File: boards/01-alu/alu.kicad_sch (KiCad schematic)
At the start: 228 parts, among them J1 BUS, Q1 2N7000, Q10 2N7000, Q100 2N7000, Q101 2N7000, Q102 2N7000, Q103 2N7000, Q104 2N7000, Q105 2N7000, Q106 2N7000, Q107 2N7000, Q108 2N7000, Q109 2N7000, Q11 2N7000, Q110 2N7000, Q111 2N7000, Q112 2N7000, Q113 2N7000, Q114 2N7000, Q115 2N7000, Q116 2N7000, Q117 2N7000, Q118 2N7000, Q119 2N7000, Q12 2N7000, Q120 2N7000, Q121 2N7000, Q122 2N7000, Q123 2N7000, Q124 2N7000, Q125 2N7000, Q126 2N7000, Q127 2N7000, Q128 2N7000, Q129 2N7000, Q13 2N7000, Q130 2N7000, Q131 2N7000, Q132 2N7000, Q133 2N7000, Q134 2N7000, Q135 2N7000, Q136 2N7000, Q137 2N7000, Q14 2N7000, Q15 2N7000, Q16 2N7000, Q17 2N7000, Q18 2N7000, Q19 2N7000, Q2 2N7000, Q20 2N7000, Q21 2N7000, Q22 2N7000, Q23 2N7000, Q24 2N7000, Q25 2N7000, Q26 2N7000, Q27 2N7000, Q28 2N7000, Q29 2N7000, Q3 2N7000, Q30 2N7000, Q31 2N7000, Q32 2N7000, Q33 2N7000, Q34 2N7000, Q35 2N7000, Q36 2N7000, Q37 2N7000, Q38 2N7000, Q39 2N7000, Q4 2N7000, Q40 2N7000, Q41 2N7000, Q42 2N7000, Q43 2N7000, Q44 2N7000, Q45 2N7000, Q46 2N7000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

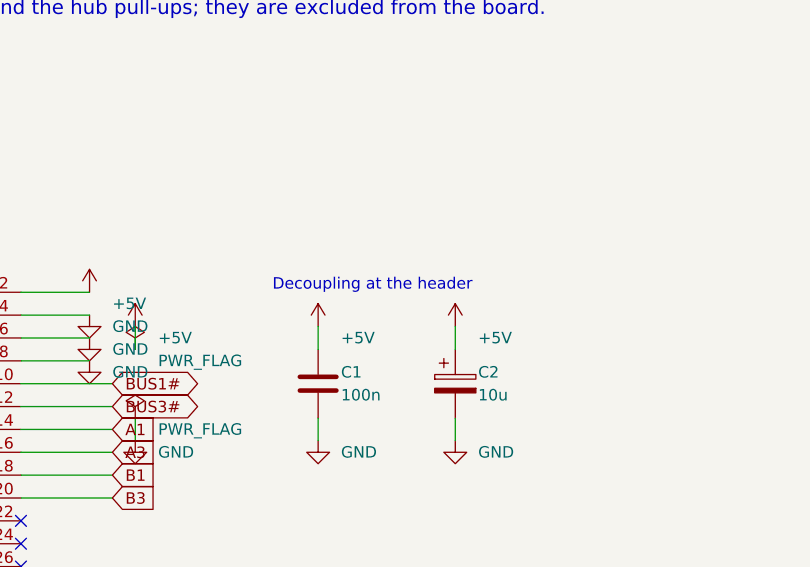
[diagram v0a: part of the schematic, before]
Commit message: Coupon, ALU and hub PCBs routed and DRC clean; fab outputs
pcb.py: power pre-routed as per-column rails from the tile geometry, fixed in
the DSN so the router cannot move them; GND pour before routing; DRC-verified
ground stitching; inset outline while routing; retries until zero unconnected.
Coupon 112x94, ALU 156x214, hub 130x98 mm. docs/bring-up.md and docs/order-1.md.

Co-Authored-By: Claude Fable 5.1 <noreply@anthropic.com>
Claude-Session: https://claude.ai/code/session_019vcbW37ERmrjZaWq55Er3J
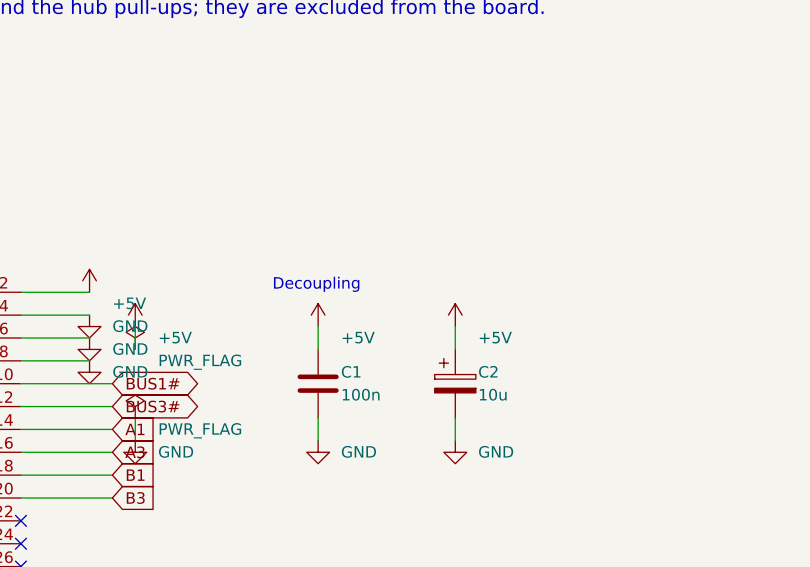
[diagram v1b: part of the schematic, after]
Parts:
- H1, H2, H3, H4: footprint MountingHole:MountingHole_3.2mm_M3 -> MountingHole:MountingHole_3.2mm_M3_Pad
- Q1, Q10, Q100, Q101, Q102, Q103, Q104, Q105, Q106, Q107, Q108, Q109, Q11, Q110, Q111, Q112, Q113, Q114, Q115, Q116, Q117, Q118, Q119, Q12, Q120, Q121, Q122, Q123, Q124, Q125, Q126, Q127, Q128, Q129, Q13, Q130, Q131, Q132, Q133, Q134, Q135, Q136, Q137, Q14, Q15, Q16, Q17, Q18, Q19, Q2, Q20, Q21, Q22, Q23, Q24, Q25, Q26, Q27, Q28, Q29, Q3, Q30, Q31, Q32, Q33, Q34, Q35, Q36, Q37, Q38, Q39, Q4, Q40, Q41, Q42, Q43, Q44, Q45, Q46, Q47, Q48, Q49, Q5, Q50, Q51, Q52, Q53, Q54, Q55, Q56, Q57, Q58, Q59, Q6, Q60, Q61, Q62, Q63, Q64, Q65, Q66, Q67, Q68, Q69, Q7, Q70, Q71, Q72, Q73, Q74, Q75, Q76, Q77, Q78, Q79, Q8, Q80, Q81, Q82, Q83, Q84, Q85, Q86, Q87, Q88, Q89, Q9, Q90, Q91, Q92, Q93, Q94, Q95, Q96, Q97, Q98, Q99: footprint Package_TO_SOT_THT:TO-92_Inline -> Package_TO_SOT_THT:TO-92_Inline_Wide
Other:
- note added: "Decoupling"
- note removed: "Decoupling at the header"

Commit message: ALU v2: ONE, F0 and F1 lines give INC/DEC, AND, OR and XOR; exhaustive at four corners
233 transistors. ONE forces the B operand to 1 for INC and DEC; F1:F0 select
add/sub, and, or, xor per bit through a result mux. Testbench rewritten
around (a, b, ctl) cases and vectorised scoring; the kicad-cli export passes
all 2,304 cases at TYP, LO, HI and the mixed-threshold corner.

Co-Authored-By: Claude Fable 5.1 <noreply@anthropic.com>
Claude-Session: https://claude.ai/code/session_019vcbW37ERmrjZaWq55Er3J
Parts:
- removed J1: BUS, Connector_IDC:IDC-Header_2x25_P2.54mm_Vertical, symbol Connector_Generic:Conn_02x25_Odd_Even
- added J1: BUS, Connector_IDC:IDC-Header_2x32_P2.54mm_Vertical, symbol Connector_Generic:Conn_02x32_Odd_Even
- added Q138, Q139, Q140, Q141, Q142, Q143, Q144, Q145, Q146, Q147, Q148, Q149, Q150, Q151, Q152, Q153, Q154, Q155, Q156, Q157, Q158, Q159, Q160, Q161, Q162, Q163, Q164, Q165, Q166, Q167, Q168, Q169, Q170, Q171, Q172, Q173, Q174, Q175, Q176, Q177, Q178, Q179, Q180, Q181, Q182, Q183, Q184, Q185, Q186, Q187, Q188, Q189, Q190, Q191, Q192, Q193, Q194, Q195, Q196, Q197, Q198, Q199, Q200, Q201, Q202, Q203, Q204, Q205, Q206, Q207, Q208, Q209, Q210, Q211, Q212, Q213, Q214, Q215, Q216, Q217, Q218, Q219, Q220, Q221, Q222, Q223, Q224, Q225, Q226, Q227, Q228, Q229, Q230, Q231, Q232, Q233: 2N7000, Package_TO_SOT_THT:TO-92_Inline_Wide, symbol Transistor_FET:2N7000
- added R100, R101, R102, R103, R104, R105, R106, R107, R108, R109, R110, R111, R112, R113, R114, R115, R116, R117, R118, R119, R120, R121, R122, R123, R124, R125, R126, R127, R79, R80, R81, R82, R83, R84, R85, R86, R87, R88, R89, R90, R91, R92, R93, R94, R95, R96, R97, R98, R99: 47k, Resistor_THT:R_Axial_DIN0207_L6.3mm_D2.5mm_P5.08mm_Vertical, symbol Device:R
- added R128, R129, R130, R131, R132, R133: 1k, Resistor_THT:R_Axial_DIN0207_L6.3mm_D2.5mm_P5.08mm_Vertical, symbol Device:R
- R73, R74, R75, R76, R77, R78: value 1k -> 47k
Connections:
- net +5V: now also J1.1 (Pin_1), J1.2 (Pin_2), J1.63 (Pin_63), R100.1, R101.1, R102.1, R103.1, R104.1, R105.1, R106.1, R107.1, R108.1, R109.1, R110.1, R111.1, R112.1, R113.1, R114.1, R115.1, R116.1, R117.1, R118.1, R119.1, R120.1, R121.1, R122.1, R123.1, R124.1, R125.1, R126.1, R127.1, R128.1, R129.1, R130.1, R131.1, R132.1, R133.1, R79.1, R80.1, R81.1, R82.1, R83.1, R84.1, R85.1, R86.1, R87.1, R88.1, R89.1, R90.1, R91.1, R92.1, R93.1, R94.1, R95.1, R96.1, R97.1, R98.1, R99.1
- net A0: now also Q42.2 (G), Q56.2 (G), J1.13 (Pin_13); no longer Q30.2 (G), Q32.2 (G)
- net A1: now also Q62.2 (G), Q76.2 (G), J1.14 (Pin_14); no longer Q50.2 (G), Q52.2 (G)
- net A2: now also Q82.2 (G), Q96.2 (G), J1.15 (Pin_15); no longer Q70.2 (G), Q72.2 (G)
- net A3: now also Q102.2 (G), Q116.2 (G), J1.16 (Pin_16); no longer Q90.2 (G), Q92.2 (G)
- net B0: now also J1.17 (Pin_17)
- net B1: now also Q12.2 (G), J1.18 (Pin_18); no longer Q10.2 (G), Q9.2 (G)
- net B2: now also Q22.2 (G), J1.19 (Pin_19); no longer Q16.2 (G), Q17.2 (G)
- net B3: now also Q32.2 (G), J1.20 (Pin_20); no longer Q23.2 (G), Q24.2 (G)
- net BD0: now also Q214.3 (D), Q215.2 (G), R121.2; no longer Q118.3 (D), Q119.2 (G), R66.2
- net BD1: now also Q218.3 (D), Q219.2 (G), R123.2; no longer Q122.3 (D), Q123.2 (G), R68.2
- net BD2: now also Q222.3 (D), Q223.2 (G), R125.2; no longer Q126.3 (D), Q127.2 (G), R70.2
- net BD3: now also Q226.3 (D), Q227.2 (G), R127.2; no longer Q130.3 (D), Q131.2 (G), R72.2
- net BDN0: now also Q212.3 (D), Q214.2 (G), R120.2; no longer Q116.3 (D), Q118.2 (G), R65.2
- net BDN1: now also Q216.3 (D), Q218.2 (G), R122.2; no longer Q120.3 (D), Q122.2 (G), R67.2
- net BDN2: now also Q220.3 (D), Q222.2 (G), R124.2; no longer Q124.3 (D), Q126.2 (G), R69.2
- net BDN3: now also Q224.3 (D), Q226.2 (G), R126.2; no longer Q128.3 (D), Q130.2 (G), R71.2
- net BN0: no longer Q5.2 (G)
- net BN1: now also Q12.3 (D), Q13.2 (G), R8.2; no longer Q12.2 (G), Q9.3 (D), R6.2
- net BN2: now also Q22.3 (D), Q23.2 (G), R14.2; no longer Q16.3 (D), Q19.2 (G), R10.2
- net BN3: now also Q32.3 (D), Q33.2 (G), R20.2; no longer Q23.3 (D), Q26.2 (G), R14.2
- net BUS0#: now also J1.9 (Pin_9), Q215.3 (D); no longer Q119.3 (D)
- net BUS1#: now also J1.10 (Pin_10), Q219.3 (D); no longer Q123.3 (D)
- net BUS2#: now also J1.11 (Pin_11), Q223.3 (D); no longer Q127.3 (D)
- net BUS3#: now also J1.12 (Pin_12), Q227.3 (D); no longer Q131.3 (D)
- net C1: now also Q60.3 (D), Q70.2 (G), Q72.2 (G), Q79.2 (G), R36.2; no longer Q48.3 (D), Q58.2 (G), Q60.2 (G), Q67.2 (G), R28.2
- net C2: now also Q80.3 (D), Q90.2 (G), Q92.2 (G), Q99.2 (G), R47.2; no longer Q68.3 (D), Q78.2 (G), Q80.2 (G), Q87.2 (G), R39.2
- net C3: now also Q100.3 (D), Q110.2 (G), Q112.2 (G), Q119.2 (G), R58.2; no longer Q100.2 (G), Q107.2 (G), Q88.3 (D), Q98.2 (G), R50.2
- net C4: now also Q120.3 (D), R69.2, Q205.2 (G); no longer Q108.3 (D), Q111.2 (G), R61.2
- net CF: now also J1.37 (Pin_37), Q207.3 (D), Q232.2 (G), R118.2; no longer Q110.3 (D), Q136.2 (G), R62.2
- net EO: now also J1.40 (Pin_40), Q213.2 (G), Q217.2 (G), Q221.2 (G), Q225.2 (G); no longer Q117.2 (G), Q121.2 (G), Q125.2 (G), Q129.2 (G)
- net G0: now also Q133.2 (G), Q136.2 (G), Q56.3 (D), Q60.2 (G), R34.2; no longer Q44.3 (D), Q48.2 (G), R26.2
- net G1: now also Q76.3 (D), Q80.2 (G), R45.2, Q151.2 (G), Q154.2 (G); no longer Q64.3 (D), Q68.2 (G), R37.2
- net G2: now also Q100.2 (G), Q96.3 (D), R56.2, Q169.2 (G), Q172.2 (G); no longer Q84.3 (D), Q88.2 (G), R48.2
- net G3: now also Q116.3 (D), Q120.2 (G), R67.2, Q187.2 (G), Q190.2 (G); no longer Q104.3 (D), Q108.2 (G), R59.2
- net GND: now also Q106.1 (S), Q108.1 (S), Q12.1 (S), Q124.1 (S), Q128.1 (S), Q14.1 (S), Q17.1 (S), Q19.1 (S), Q21.1 (S), Q24.1 (S), Q3.1 (S), Q32.1 (S), Q39.1 (S), Q46.1 (S), Q48.1 (S), Q5.1 (S), Q52.1 (S), Q59.1 (S), Q66.1 (S), Q68.1 (S), Q7.1 (S), Q72.1 (S), Q79.1 (S), Q86.1 (S), Q88.1 (S), Q92.1 (S), Q99.1 (S), J1.3 (Pin_3), J1.4 (Pin_4), J1.6 (Pin_6), J1.64 (Pin_64), J1.8 (Pin_8), Q138.1 (S), Q140.1 (S), Q142.1 (S), Q144.1 (S), Q147.1 (S), Q148.1 (S), Q150.1 (S), Q151.1 (S), Q152.1 (S), Q154.1 (S), Q156.1 (S), Q158.1 (S), Q160.1 (S), Q162.1 (S), Q165.1 (S), Q166.1 (S), Q168.1 (S), Q169.1 (S), Q170.1 (S), Q172.1 (S), Q174.1 (S), Q176.1 (S), Q178.1 (S), Q180.1 (S), Q183.1 (S), Q184.1 (S), Q186.1 (S), Q187.1 (S), Q188.1 (S), Q190.1 (S), Q192.1 (S), Q194.1 (S), Q196.1 (S), Q198.1 (S), Q201.1 (S), Q202.1 (S), Q204.1 (S), Q206.1 (S), Q207.1 (S), Q208.1 (S), Q209.1 (S), Q210.1 (S), Q211.1 (S), Q213.1 (S), Q214.1 (S), Q215.1 (S), Q217.1 (S), Q218.1 (S), Q219.1 (S), Q221.1 (S), Q222.1 (S), Q223.1 (S), Q225.1 (S), Q226.1 (S), Q227.1 (S), Q228.1 (S), Q229.1 (S), Q230.1 (S), Q231.1 (S), Q232.1 (S), Q233.1 (S); no longer Q100.1 (S), Q111.1 (S), Q118.1 (S), Q130.1 (S), Q135.1 (S), Q137.1 (S), Q16.1 (S), Q18.1 (S), Q20.1 (S), Q30.1 (S), Q36.1 (S), Q38.1 (S), Q40.1 (S), Q51.1 (S), Q56.1 (S), Q58.1 (S), Q6.1 (S), Q60.1 (S), Q71.1 (S), Q76.1 (S), Q78.1 (S), Q8.1 (S), Q80.1 (S), Q91.1 (S), Q96.1 (S), Q98.1 (S)
- net P0: now also Q134.2 (G), Q47.3 (D), Q48.3 (D), Q49.2 (G), Q51.2 (G), Q58.2 (G), R29.2, Q144.2 (G); no longer Q35.3 (D), Q36.3 (D), Q37.2 (G), Q39.2 (G), Q46.2 (G), R21.2
- net P0_a: now also Q44.3 (D), Q46.2 (G), R27.2; no longer Q32.3 (D), Q34.2 (G), R19.2
- net P0_d: now also Q46.3 (D), Q48.2 (G), R28.2; no longer Q34.3 (D), Q36.2 (G), R20.2
- net P0_n: now also Q42.3 (D), Q43.3 (D), Q47.2 (G), R26.2; no longer Q30.3 (D), Q31.3 (D), Q35.2 (G), R18.2
- net P1: now also Q67.3 (D), Q68.3 (D), Q69.2 (G), Q71.2 (G), Q78.2 (G), R40.2, Q152.2 (G), Q162.2 (G); no longer Q55.3 (D), Q56.3 (D), Q57.2 (G), Q59.2 (G), Q66.2 (G), R32.2
- net P1_a: now also Q64.3 (D), Q66.2 (G), R38.2; no longer Q52.3 (D), Q54.2 (G), R30.2
- net P1_d: now also Q66.3 (D), Q68.2 (G), R39.2; no longer Q54.3 (D), Q56.2 (G), R31.2
- net P1_n: now also Q62.3 (D), Q63.3 (D), Q67.2 (G), R37.2; no longer Q50.3 (D), Q51.3 (D), Q55.2 (G), R29.2
- net P2: now also Q87.3 (D), Q88.3 (D), Q89.2 (G), Q91.2 (G), Q98.2 (G), R51.2, Q170.2 (G), Q180.2 (G); no longer Q75.3 (D), Q76.3 (D), Q77.2 (G), Q79.2 (G), Q86.2 (G), R43.2
- net P2_a: now also Q84.3 (D), Q86.2 (G), R49.2; no longer Q72.3 (D), Q74.2 (G), R41.2
- net P2_d: now also Q86.3 (D), Q88.2 (G), R50.2; no longer Q74.3 (D), Q76.2 (G), R42.2
- net P2_n: now also Q82.3 (D), Q83.3 (D), Q87.2 (G), R48.2; no longer Q70.3 (D), Q71.3 (D), Q75.2 (G), R40.2
- net P3: now also Q107.3 (D), Q108.3 (D), Q109.2 (G), Q111.2 (G), Q118.2 (G), R62.2, Q188.2 (G), Q198.2 (G); no longer Q106.2 (G), Q95.3 (D), Q96.3 (D), Q97.2 (G), Q99.2 (G), R54.2
- net P3_a: now also Q104.3 (D), Q106.2 (G), R60.2; no longer Q92.3 (D), Q94.2 (G), R52.2
- net P3_d: now also Q106.3 (D), Q108.2 (G), R61.2; no longer Q94.3 (D), Q96.2 (G), R53.2
- net P3_n: now also Q102.3 (D), Q103.3 (D), Q107.2 (G), R59.2; no longer Q90.3 (D), Q91.3 (D), Q95.2 (G), R51.2
- net S0: now also Q54.3 (D), Q55.3 (D), R33.2, Q138.2 (G); no longer Q112.2 (G), Q116.2 (G), Q135.2 (G), Q42.3 (D), Q43.3 (D), R25.2
- net S0_a: now also Q51.3 (D), Q53.2 (G), R31.2; no longer Q39.3 (D), Q41.2 (G), R23.2
- net S0_d: now also Q53.3 (D), Q55.2 (G), R32.2; no longer Q41.3 (D), Q43.2 (G), R24.2
- net S0_n: now also Q49.3 (D), Q50.3 (D), Q54.2 (G), R30.2; no longer Q37.3 (D), Q38.3 (D), Q42.2 (G), R22.2
- net S1: now also Q74.3 (D), Q75.3 (D), R44.2, Q156.2 (G); no longer Q113.2 (G), Q120.2 (G), Q134.2 (G), Q62.3 (D), Q63.3 (D), R36.2
- net S1_a: now also Q71.3 (D), Q73.2 (G), R42.2; no longer Q59.3 (D), Q61.2 (G), R34.2
- net S1_d: now also Q73.3 (D), Q75.2 (G), R43.2; no longer Q61.3 (D), Q63.2 (G), R35.2
- net S1_n: now also Q69.3 (D), Q70.3 (D), Q74.2 (G), R41.2; no longer Q57.3 (D), Q58.3 (D), Q62.2 (G), R33.2
- net S2: now also Q94.3 (D), Q95.3 (D), R55.2, Q174.2 (G); no longer Q114.2 (G), Q124.2 (G), Q133.2 (G), Q82.3 (D), Q83.3 (D), R47.2
- net S2_a: now also Q91.3 (D), Q93.2 (G), R53.2; no longer Q79.3 (D), Q81.2 (G), R45.2
- net S2_d: now also Q93.3 (D), Q95.2 (G), R54.2; no longer Q81.3 (D), Q83.2 (G), R46.2
- net S2_n: now also Q89.3 (D), Q90.3 (D), Q94.2 (G), R52.2; no longer Q77.3 (D), Q78.3 (D), Q82.2 (G), R44.2
- net S3: now also Q114.3 (D), Q115.3 (D), R66.2, Q192.2 (G); no longer Q102.3 (D), Q103.3 (D), Q115.2 (G), Q128.2 (G), Q132.2 (G), R58.2
- net S3_a: now also Q111.3 (D), Q113.2 (G), R64.2; no longer Q101.2 (G), Q99.3 (D), R56.2
- net S3_d: now also Q113.3 (D), Q115.2 (G), R65.2; no longer Q101.3 (D), Q103.2 (G), R57.2
- net S3_n: now also Q109.3 (D), Q110.3 (D), Q114.2 (G), R63.2; no longer Q102.2 (G), Q97.3 (D), Q98.3 (D), R55.2
- net SUB: now also Q19.2 (G), Q29.2 (G), Q39.2 (G), Q50.2 (G), Q52.2 (G), Q59.2 (G), Q9.2 (G), J1.39 (Pin_39); no longer Q13.2 (G), Q20.2 (G), Q27.2 (G), Q38.2 (G), Q40.2 (G), Q47.2 (G), Q6.2 (G)
- net SUBN: now also Q17.2 (G), Q27.2 (G), Q37.2 (G), Q7.2 (G); no longer Q11.2 (G), Q18.2 (G), Q25.2 (G), Q4.2 (G)
- net T0: now also Q58.3 (D), Q61.2 (G), R35.2; no longer Q46.3 (D), Q49.2 (G), R27.2
- net T1: now also Q78.3 (D), Q81.2 (G), R46.2; no longer Q66.3 (D), Q69.2 (G), R38.2
- net T2: now also Q101.2 (G), Q98.3 (D), R57.2; no longer Q86.3 (D), Q89.2 (G), R49.2
- net T3: now also Q118.3 (D), Q121.2 (G), R68.2; no longer Q106.3 (D), Q109.2 (G), R60.2
- net XB0: now also Q10.3 (D), Q43.2 (G), Q57.2 (G), R7.2; no longer Q31.2 (G), Q33.2 (G), Q7.3 (D), R5.2
- net XB1: now also Q20.3 (D), Q63.2 (G), Q77.2 (G), R13.2; no longer Q14.3 (D), Q51.2 (G), Q53.2 (G), R9.2
- net XB2: now also Q30.3 (D), Q83.2 (G), Q97.2 (G), R19.2; no longer Q21.3 (D), Q71.2 (G), Q73.2 (G), R13.2
- net XB3: now also Q103.2 (G), Q117.2 (G), Q40.3 (D), R25.2; no longer Q28.3 (D), Q91.2 (G), Q93.2 (G), R17.2
- net XBA0: now also Q10.2 (G), Q6.3 (D), R5.2; no longer Q3.3 (D), Q7.2 (G), R3.2
- net XBA1: now also Q16.3 (D), Q20.2 (G), R11.2; no longer Q10.3 (D), Q14.2 (G), R7.2
- net XBA2: now also Q26.3 (D), Q30.2 (G), R17.2; no longer Q17.3 (D), Q21.2 (G), R11.2
- net XBA3: now also Q36.3 (D), Q40.2 (G), R23.2; no longer Q24.3 (D), Q28.2 (G), R15.2
- net XBB0: now also Q11.2 (G), Q8.3 (D), R6.2; no longer Q5.3 (D), Q8.2 (G), R4.2
- net XBB1: now also Q18.3 (D), Q21.2 (G), R12.2; no longer Q12.3 (D), Q15.2 (G), R8.2
- net XBB2: now also Q28.3 (D), Q31.2 (G), R18.2; no longer Q19.3 (D), Q22.2 (G), R12.2
- net XBB3: now also Q38.3 (D), Q41.2 (G), R24.2; no longer Q26.3 (D), Q29.2 (G), R16.2
- net ZF: now also J1.38 (Pin_38), Q208.3 (D), Q209.3 (D), Q210.3 (D), Q211.3 (D), Q233.2 (G), R119.2; no longer Q112.3 (D), Q113.3 (D), Q114.3 (D), Q115.3 (D), Q137.2 (G), R64.2
- net at D5.2 (A): now also R132.2; no longer R77.2
- net BB1N: now reaches Q15.3 (D)
- net BB1N: now also Q18.2 (G), R10.2; no longer Q14.1 (S)
- net at D1.2 (A): now also R128.2; no longer R73.2
- net BB2N: now reaches Q25.3 (D)
- net BB2N: now also Q28.2 (G), R16.2; no longer Q24.1 (S)
- net at D1.1 (K): now also Q228.3 (D); no longer Q132.3 (D)
- net at D5.1 (K): now also Q232.3 (D); no longer Q136.3 (D)
- net BB0N: now reaches Q4.3 (D)
- net BB0N: now also Q3.3 (D), Q5.2 (G), Q8.2 (G), R3.2; no longer Q3.1 (S)
- net BB3: now reaches Q33.3 (D)
- net BB3: now also Q34.3 (D), Q35.2 (G), Q36.2 (G), R21.2; no longer Q32.1 (S)
- net at D2.1 (K): now also Q229.3 (D); no longer Q133.3 (D)
- net at D2.2 (A): now also R129.2; no longer R74.2
- net at D4.1 (K): now also Q231.3 (D); no longer Q135.3 (D)
- net at D4.2 (A): now also R131.2; no longer R76.2
- net FS: now reaches Q125.3 (D)
- net FS: now also Q124.3 (D), Q137.2 (G), R72.2, Q155.2 (G), Q173.2 (G), Q191.2 (G), Q206.2 (G); no longer Q124.1 (S)
- net at D6.1 (K): now also Q233.3 (D); no longer Q137.3 (D)
- net FO: now reaches Q129.3 (D)
- net FO: now also Q128.3 (D), R74.2, Q141.2 (G), Q159.2 (G), Q177.2 (G), Q195.2 (G); no longer Q128.1 (S)
- net at D6.2 (A): now also R133.2; no longer R78.2
- net at D3.1 (K): now also Q230.3 (D); no longer Q134.3 (D)
- net BB1: now reaches Q13.3 (D)
- net BB1: now also Q14.3 (D), Q15.2 (G), Q16.2 (G), R9.2; no longer Q12.1 (S)
- net at D3.2 (A): now also R130.2; no longer R75.2
- removed net C4N: Q110.2 (G), Q111.3 (D), R63.2
- new net: Q130.1 (S), Q131.3 (D)
- new net: Q189.1 (S), Q190.3 (D)
- new net: Q60.1 (S), Q61.3 (D)
- new net: Q139.1 (S), Q140.3 (D)
- new net: Q212.1 (S), Q213.3 (D)
- new net: Q195.1 (S), Q196.3 (D)
- new net: Q36.1 (S), Q37.3 (D)
- new net: Q8.1 (S), Q9.3 (D)
- new net: Q58.1 (S), Q59.3 (D)
- new net: Q91.1 (S), Q92.3 (D)
- new net: Q216.1 (S), Q217.3 (D)
- new net: Q145.1 (S), Q146.3 (D)
- new net: Q157.1 (S), Q158.3 (D)
- new net: Q182.1 (S), Q183.3 (D)
- new net: Q181.1 (S), Q182.3 (D)
- new net: Q177.1 (S), Q178.3 (D)
- new net: Q38.1 (S), Q39.3 (D)
- new net: Q6.1 (S), Q7.3 (D)
- new net: Q197.1 (S), Q198.3 (D)
- new net: Q18.1 (S), Q19.3 (D)
- new net: Q100.1 (S), Q101.3 (D)
- new net: Q118.1 (S), Q119.3 (D)
- new net: Q51.1 (S), Q52.3 (D)
- new net: Q98.1 (S), Q99.3 (D)
- new net: Q155.1 (S), Q156.3 (D)
- new net: Q179.1 (S), Q180.3 (D)
- new net: Q16.1 (S), Q17.3 (D)
- new net: Q76.1 (S), Q77.3 (D)
- new net: Q171.1 (S), Q172.3 (D)
- new net: Q137.1 (S), Q138.3 (D)
- new net: Q80.1 (S), Q81.3 (D)
- new net: Q161.1 (S), Q162.3 (D)
- new net: Q40.1 (S), Q41.3 (D)
- new net: Q71.1 (S), Q72.3 (D)
- new net: Q175.1 (S), Q176.3 (D)
- new net: Q173.1 (S), Q174.3 (D)
- new net: Q193.1 (S), Q194.3 (D)
- new net: Q78.1 (S), Q79.3 (D)
- new net: Q149.1 (S), Q150.3 (D)
- new net: Q191.1 (S), Q192.3 (D)
- new net: Q224.1 (S), Q225.3 (D)
- new net: Q135.1 (S), Q136.3 (D)
- new net: Q203.1 (S), Q204.3 (D)
- new net: Q167.1 (S), Q168.3 (D)
- new net: Q56.1 (S), Q57.3 (D)
- new net: Q199.1 (S), Q200.3 (D)
- new net: Q185.1 (S), Q186.3 (D)
- new net: Q159.1 (S), Q160.3 (D)
- new net: Q205.1 (S), Q206.3 (D)
- new net: Q220.1 (S), Q221.3 (D)
- new net: Q30.1 (S), Q31.3 (D)
- new net: Q164.1 (S), Q165.3 (D)
- new net: Q111.1 (S), Q112.3 (D)
- new net: Q146.1 (S), Q147.3 (D)
- new net: Q153.1 (S), Q154.3 (D)
- new net: Q200.1 (S), Q201.3 (D)
- new net: Q20.1 (S), Q21.3 (D)
- new net: Q143.1 (S), Q144.3 (D)
- new net: Q141.1 (S), Q142.3 (D)
- new net: Q96.1 (S), Q97.3 (D)
- new net: Q163.1 (S), Q164.3 (D)
- new net AND0: Q133.3 (D), Q140.2 (G), R77.2
- new net AND1: Q151.3 (D), Q158.2 (G), R87.2
- new net AND2: Q169.3 (D), Q176.2 (G), R97.2
- new net AND3: Q187.3 (D), Q194.2 (G), R107.2
- new net BB0: Q5.3 (D), Q6.2 (G), R4.2
- new net BB2: Q23.3 (D), Q24.3 (D), Q25.2 (G), Q26.2 (G), R15.2
- new net BB3N: Q35.3 (D), Q38.2 (G), R22.2
- new net CFN: Q205.3 (D), Q207.2 (G), R117.2
- new net F0: J1.60 (Pin_60), Q122.2 (G), Q125.2 (G), Q129.2 (G), Q131.2 (G)
- new net F0N: Q122.3 (D), Q127.2 (G), R70.2
- new net F1: J1.61 (Pin_61), Q123.2 (G), Q124.2 (G), Q126.2 (G), Q130.2 (G)
- new net F1N: Q123.3 (D), Q128.2 (G), R71.2
- new net FA: Q126.3 (D), Q127.3 (D), Q139.2 (G), Q157.2 (G), Q175.2 (G), Q193.2 (G), R73.2
- new net FX: Q132.3 (D), Q143.2 (G), Q161.2 (G), Q179.2 (G), Q197.2 (G), R76.2
- new net FXN: Q130.3 (D), Q132.2 (G), R75.2
- new net ONE: J1.59 (Pin_59), Q14.2 (G), Q24.2 (G), Q34.2 (G), Q4.2 (G)
- new net OR0: Q135.3 (D), Q142.2 (G), R79.2
- new net OR1: Q153.3 (D), Q160.2 (G), R89.2
- new net OR2: Q171.3 (D), Q178.2 (G), R99.2
- new net OR3: Q189.3 (D), Q196.2 (G), R109.2
- new net PN0: Q134.3 (D), Q135.2 (G), R78.2
- new net PN1: Q152.3 (D), Q153.2 (G), R88.2
- new net PN2: Q170.3 (D), Q171.2 (G), R98.2
- new net PN3: Q188.3 (D), Q189.2 (G), R108.2
- new net R0: Q149.3 (D), Q208.2 (G), Q212.2 (G), Q231.2 (G), R86.2
- new net R1: Q167.3 (D), Q209.2 (G), Q216.2 (G), Q230.2 (G), R96.2
- new net R2: Q185.3 (D), Q210.2 (G), Q220.2 (G), Q229.2 (G), R106.2
- new net R3: Q203.3 (D), Q211.2 (G), Q224.2 (G), Q228.2 (G), R116.2
- new net RA0: Q139.3 (D), Q146.2 (G), R81.2
- new net RA1: Q157.3 (D), Q164.2 (G), R91.2
- new net RA2: Q175.3 (D), Q182.2 (G), R101.2
- new net RA3: Q193.3 (D), Q200.2 (G), R111.2
- new net RM0: Q145.3 (D), Q148.2 (G), R84.2
- new net RM1: Q163.3 (D), Q166.2 (G), R94.2
- new net RM2: Q181.3 (D), Q184.2 (G), R104.2
- new net RM3: Q199.3 (D), Q202.2 (G), R114.2
- new net RMN0: Q148.3 (D), Q149.2 (G), R85.2
- new net RMN1: Q166.3 (D), Q167.2 (G), R95.2
- new net RMN2: Q184.3 (D), Q185.2 (G), R105.2
- new net RMN3: Q202.3 (D), Q203.2 (G), R115.2
- new net RO0: Q141.3 (D), Q147.2 (G), R82.2
- new net RO1: Q159.3 (D), Q165.2 (G), R92.2
- new net RO2: Q177.3 (D), Q183.2 (G), R102.2
- new net RO3: Q195.3 (D), Q201.2 (G), R112.2
- new net RS0: Q137.3 (D), Q145.2 (G), R80.2
- new net RS1: Q155.3 (D), Q163.2 (G), R90.2
- new net RS2: Q173.3 (D), Q181.2 (G), R100.2
- new net RS3: Q191.3 (D), Q199.2 (G), R110.2
- new net RX0: Q143.3 (D), Q150.2 (G), R83.2
- new net RX1: Q161.3 (D), Q168.2 (G), R93.2
- new net RX2: Q179.3 (D), Q186.2 (G), R103.2
- new net RX3: Q197.3 (D), Q204.2 (G), R113.2
- no-connect marks 26 -> 37
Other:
- note added: "B INPUT: BB = B, or 0001 when ONE=1 (INC, DEC). Then the conditional invert: XB = BB when SUB=0, NOT BB when SUB=1 (two's complement: A - B = A + NOT B + 1, the +1 is SUB fed into the carry-in)"
- note added: "BUS DRIVERS: pull BUS_i# low when EO=1 and R_i=1 (open drain, pull-ups live on the hub board)"
- note added: "Cell: 2N7000 + 47k pull-up (NMOS, see docs/gate-cell.md). 233 transistors, 133 resistors, 6 LEDs. Inputs from the bus header: A3..A0, B3..B0 (register contents), SUB (1 = subtract), ONE (B input replaced by 0001: INC, DEC), F1 F0 (function), EO (1 = drive the result onto the bus). Outputs: CF (carry out; for SUB, 1 = no borrow; 0 for the logic functions), ZF (result is zero), BUS3#..BUS0# (open-d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"
- note added: "FLAGS: CF = carry out of bit 3, only for add/sub (0 for the logic functions); ZF = all result bits zero"
- note added: "FUNCTION DECODE: FS = add/sub (F1 F0 = 00), FA = and (01), FO = or (10), FX = xor (11)"
- note added: "INDICATORS: result R3..R0, CF, ZF"
- note added: "LED_R0"
- note added: "LED_R1"
- note added: "LED_R2"
- note added: "LED_R3"
- note added: "NIBBLE BOARD 01 - ALU: 4-bit adder/subtractor, AND, OR, XOR, with carry and zero flags"
- note added: "RESULT SELECT, per bit: R = FS.S + FA.AND + FO.OR + FX.P. NAND-NAND form with the four-way OR split as NAND3 then NAND2 (never more than three transistors in series)"
- note added: "RIPPLE-CARRY FULL ADDERS, bit 0 to bit 3: P = A xor XB, S = P xor Cin, Cout = A.XB + P.Cin. G = NAND(A, XB) is also NOT (A and XB), P is A xor XB, and A or XB = NAND(NOT P, G): the logic functions fall out of the adder"
- note removed: "B CONDITIONAL INVERT: XB = B when SUB=0, NOT B when SUB=1 (two's complement: A - B = A + NOT B + 1, the +1 is SUB fed into the carry-in)"
- note removed: "BUS DRIVERS: pull BUS_i# low when EO=1 and S_i=1 (open drain, pull-ups live on the hub board)"
- note removed: "Cell: 2N7000 + 47k pull-up (NMOS, see docs/gate-cell.md). 137 transistors, 78 resistors, 6 LEDs. Inputs from the bus header: A3..A0, B3..B0 (register contents), SUB (1 = subtract), EO (1 = drive the result onto the bus). Outputs: CF (carry out; for SUB, 1 = no borrow), ZF (result is zero), BUS3#..BUS0# (open-drain, active-low: pulled low where the result bit is 1 and EO = 1). Result S = A + (B xo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"
- note removed: "FLAGS: CF = carry out of bit 3, ZF = all sum bits zero"
- note removed: "INDICATORS: result S3..S0, CF, ZF"
- note removed: "LED_S0"
- note removed: "LED_S1"
- note removed: "LED_S2"
- note removed: "LED_S3"
- note removed: "NIBBLE BOARD 01 - ALU: 4-bit two's-complement adder/subtractor with carry and zero flags"
- note removed: "RIPPLE-CARRY FULL ADDERS, bit 0 to bit 3: P = A xor XB, S = P xor Cin, Cout = A.XB + P.Cin"
